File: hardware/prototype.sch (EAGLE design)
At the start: 33 parts, among them IC1 PCA82C251, IC2 ATMEGA328P-PU, Q3 BS170

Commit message: Smaller PCB, also the placement of the RASPI port has been corrected and the Serial port error
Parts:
- removed SW1: (no value), special:SW_DIP-4
- ATMEGA168-20PU: value ATMEGA328P-PU -> ATMEGA168V-10P
- MCP2551: value PCA82C251 -> PCA82C250
- OSC1: value (none) -> 16MHz
- renumbered IC1 to MCP2551, IC2 to ATMEGA168-20PU, ISP1 to ICSP, LED3 to RXBUF1, LED4 to RXBUF2, Q1 to 16MHZ, Q2 to OSC1, S1 to RESET, SV1 to RASPI, U$1 to MCP2515-I/P, X1 to CANPORT
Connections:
- removed net N$12: ATMEGA168-20PU.(PCI4/MISO)PB4, ICSP.MISO, SW1.3
- removed net N$13: ATMEGA168-20PU.(PCI3/MOSI/OC2A)PB3, ICSP.MOSI, SW1.2
- removed net N$14: ATMEGA168-20PU.(PCI5/SCK)PB5, ICSP.SCK, SW1.4
- removed net N$21: ATMEGA168-20PU.(PCI16/RXD)PD0, R4.1
- removed net N$28: ATMEGA168-20PU.(PCI2/SS/OC1B)PB2, SW1.1
- new net N$11: ATMEGA168-20PU.(PCI17/TXD)PD1, R4.1
- net N$10: now also ATMEGA168-20PU.(PCI2/SS/OC1B)PB2; no longer SW1.8
- net N$15: now also ATMEGA168-20PU.(PCI5/SCK)PB5, ICSP.SCK; no longer SW1.5
- net N$23: now also ATMEGA168-20PU.(PCI16/RXD)PD0; no longer ATMEGA168-20PU.(PCI17/TXD)PD1
- net N$26: now also ATMEGA168-20PU.(PCI4/MISO)PB4, ICSP.MISO; no longer SW1.6
- net N$27: now also ATMEGA168-20PU.(PCI3/MOSI/OC2A)PB3, ICSP.MOSI; no longer SW1.7

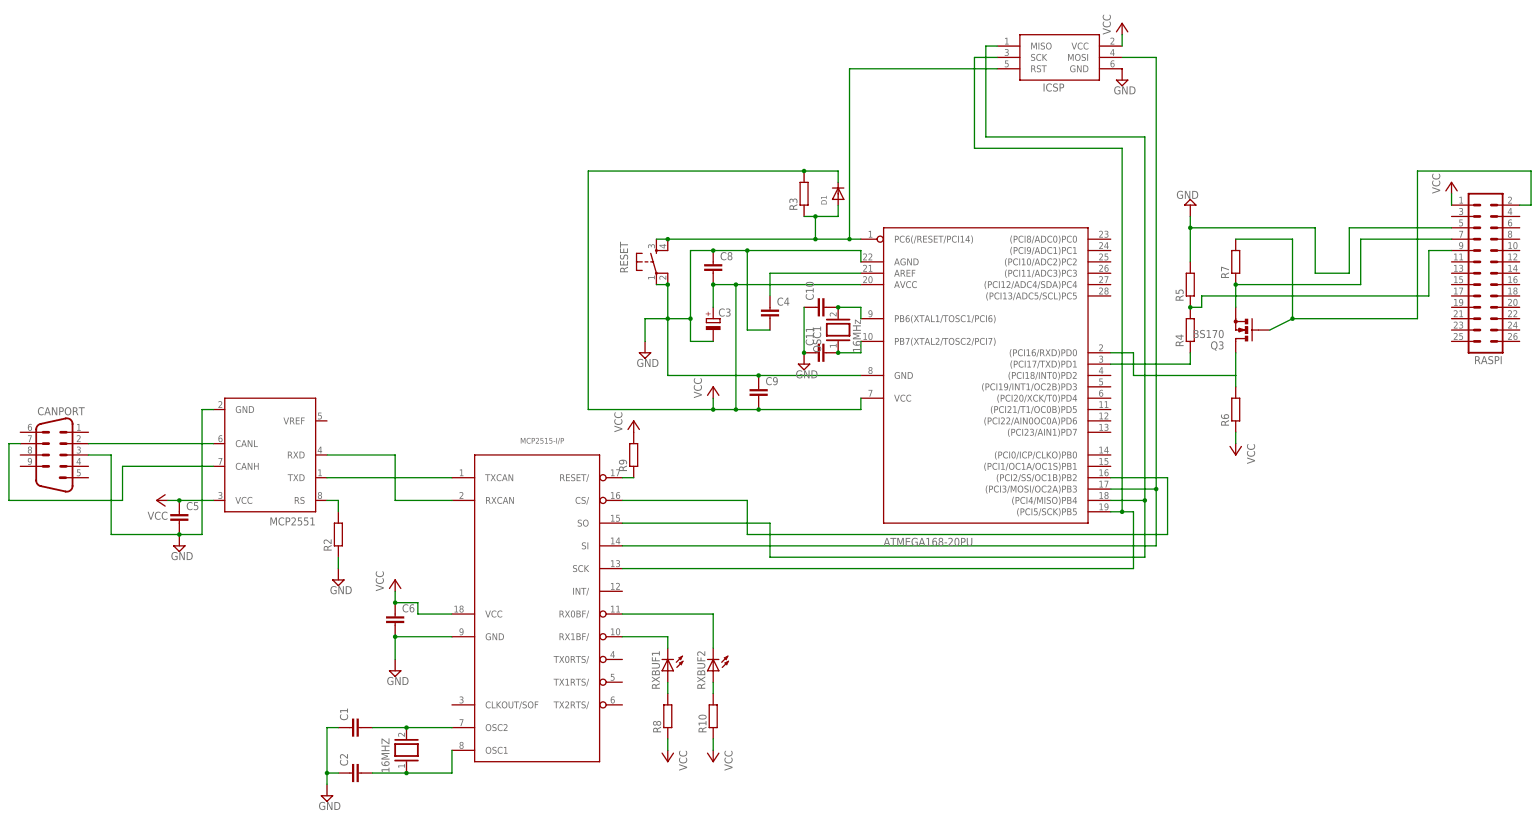
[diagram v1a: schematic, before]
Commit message: Added gerbers for DirtyPCBs and OSHpark.
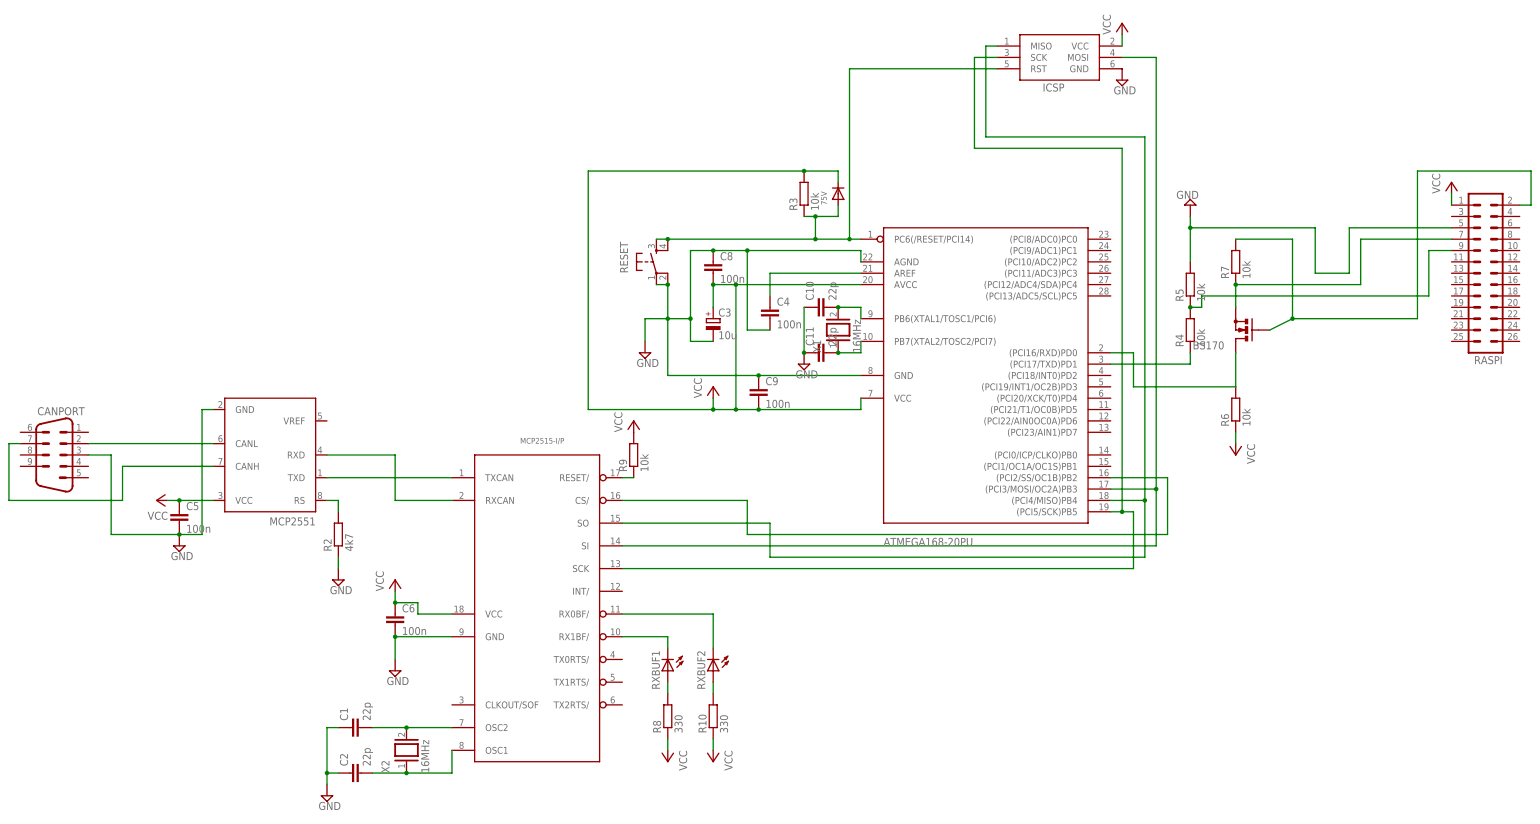
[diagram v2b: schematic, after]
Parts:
- C1, C10, C11, C2: value (none) -> 22p
- C3: value (none) -> 10u
- C4, C5, C6, C8, C9: value (none) -> 100n
- R10, R8: value (none) -> 330
- R2: value (none) -> 4k7
- R3, R4, R5, R6, R7, R9: value (none) -> 10k
- X2: value (none) -> 16MHz
- renumbered 16MHZ to X2, D1 to 75V, OSC1 to X1, Q3 to BS170
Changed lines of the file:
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@@
 <part name="P+7" library="supply1" deviceset="VCC" device=""/>
 <part name="SUPPLY5" library="supply2" deviceset="GND" device=""/>
-<part name="C5" library="rcl" deviceset="C-EU" device="050-025X075"/>
-<part name="C6" library="rcl" deviceset="C-EU" device="050-025X075"/>
-<part name="C1" library="rcl" deviceset="C-EU" device="050-025X075"/>
-<part name="C2" library="rcl" deviceset="C-EU" device="050-025X075"/>
-<part name="R2" library="rcl" deviceset="R-EU_" device="0204/7"/>
-<part name="R8" library="rcl" deviceset="R-EU_" device="0204/7"/>
-<part name="R9" library="rcl" deviceset="R-EU_" device="0204/7"/>
-<part name="R10" library="rcl" deviceset="R-EU_" device="0204/7"/>
-<part name="16MHZ" library="special" deviceset="XTAL/S" device=""/>
+<part name="C5" library="rcl" deviceset="C-EU" device="050-025X075" value="100n"/>
+<part name="C6" library="rcl" deviceset="C-EU" device="050-025X075" value="100n"/>
+<part name="C1" library="rcl" deviceset="C-EU" device="050-025X075" value="22p"/>
+<part name="C2" library="rcl" deviceset="C-EU" device="050-025X075" value="22p"/>
+<part name="R2" library="rcl" deviceset="R-EU_" device="0204/7" value="4k7"/>
+<part name="R8" library="rcl" deviceset="R-EU_" device="0204/7" value="330"/>
+<part name="R9" library="rcl" deviceset="R-EU_" device="0204/7" value="10k"/>
+<part name="R10" library="rcl" deviceset="R-EU_" device="0204/7" value="330"/>
+<part name="X2" library="special" deviceset="XTAL/S" device="" value="16MHz"/>
 <part name="ATMEGA168-20PU" library="adafruit" deviceset="ATMEGA168*P" device="" technology="V-10" value=""/>
-<part name="C4" library="rcl" deviceset="C-EU" device="050-025X075"/>
-<part name="C8" library="rcl" deviceset="C-EU" device="050-025X075"/>
-<part name="C9" library="rcl" deviceset="C-EU" device="050-025X075"/>
+<part name="C4" library="rcl" deviceset="C-EU" device="050-025X075" value="100n"/>
+<part name="C8" library="rcl" deviceset="C-EU" device="050-025X075" value="100n"/>
+<part name="C9" library="rcl" deviceset="C-EU" device="050-025X075" value="100n"/>
 <part name="RESET" library="switch-tact" deviceset="DTS-6" device="" value=""/>
 <part name="P+1" library="supply1" deviceset="VCC" device=""/>
 <part name="SUPPLY6" library="supply2" deviceset="GND" device=""/>
-<part name="C3" library="rcl" deviceset="CPOL-EU" device="E2-5"/>
-<part name="OSC1" library="special" deviceset="XTAL/S" device="" value="16MHz"/>
-<part name="C10" library="rcl" deviceset="C-EU" device="050-025X075"/>
-<part name="C11" library="rcl" deviceset="C-EU" device="050-025X075"/>
+<part name="C3" library="rcl" deviceset="CPOL-EU" device="E2-5" value="10u"/>
+<part name="X1" library="special" deviceset="XTAL/S" device="" value="16MHz"/>
+<part name="C10" library="rcl" deviceset="C-EU" device="050-025X075" value="22p"/>
+<part name="C11" library="rcl" deviceset="C-EU" device="050-025X075" value="22p"/>
 <part name="SUPPLY7" library="supply2" deviceset="GND" device=""/>
-<part name="R3" library="rcl" deviceset="R-EU_" device="0204/7"/>
-<part name="D1" library="adafruit" deviceset="DIODE" device="DO-1N4148"/>
-<part name="Q3" library="transistor-small-signal" deviceset="BS170" device=""/>
-<part name="R4" library="rcl" deviceset="R-EU_" device="0204/7"/>
-<part name="R5" library="rcl" deviceset="R-EU_" device="0204/7"/>
+<part name="R3" library="rcl" deviceset="R-EU_" device="0204/7" value="10k"/>
+<part name="75V" library="adafruit" deviceset="DIODE" device="DO-1N4148"/>
+<part name="BS170" library="transistor-small-signal" deviceset="BS170" device="" value=""/>
+<part name="R4" library="rcl" deviceset="R-EU_" device="0204/7" value="10k"/>
+<part name="R5" library="rcl" deviceset="R-EU_" device="0204/7" value="10k"/>
 <part name="SUPPLY8" library="supply2" deviceset="GND" device=""/>
-<part name="R6" library="rcl" deviceset="R-EU_" device="0204/7"/>
+<part name="R6" library="rcl" deviceset="R-EU_" device="0204/7" value="10k"/>
 <part name="P+2" library="supply1" deviceset="VCC" device=""/>
-<part name="R7" library="rcl" deviceset="R-EU_" device="0204/7"/>
+<part name="R7" library="rcl" deviceset="R-EU_" device="0204/7" value="10k"/>
 <part name="RASPI" library="con-lstb" deviceset="MA13-2" device=""/>
 <part name="ICSP" library="adafruit" deviceset="AVRISP" device="-6"/>
@@
 <instance part="R9" gate="G$1" x="142.24" y="63.5" rot="R90"/>
 <instance part="R10" gate="G$1" x="160.02" y="5.08" rot="R90"/>
-<instance part="16MHZ" gate="G$1" x="91.44" y="-2.54" rot="R90"/>
+<instance part="X2" gate="G$1" x="91.44" y="-2.54" rot="R90"/>
 <instance part="ATMEGA168-20PU" gate="G$1" x="215.9" y="83.82"/>
 <instance part="C4" gate="G$1" x="172.72" y="96.52"/>
@@
 <instance part="SUPPLY6" gate="GND" x="144.78" y="86.36"/>
 <instance part="C3" gate="G$1" x="160.02" y="93.98"/>
-<instance part="OSC1" gate="G$1" x="187.96" y="91.44" rot="R90"/>
+<instance part="X1" gate="G$1" x="187.96" y="91.44" rot="R90"/>
 <instance part="C10" gate="G$1" x="182.88" y="96.52" rot="R90"/>
 <instance part="C11" gate="G$1" x="182.88" y="86.36" rot="R90"/>
 <instance part="SUPPLY7" gate="GND" x="180.34" y="83.82"/>
 <instance part="R3" gate="G$1" x="180.34" y="121.92" rot="R90"/>
-<instance part="D1" gate="G$1" x="187.96" y="121.92" rot="R90"/>
-<instance part="Q3" gate="1" x="279.4" y="91.44" rot="R180"/>
+<instance part="75V" gate="G$1" x="187.96" y="121.92" rot="R90"/>
+<instance part="BS170" gate="1" x="279.4" y="91.44" rot="R180"/>
 <instance part="R4" gate="G$1" x="266.7" y="91.44" rot="R90"/>
 <instance part="R5" gate="G$1" x="266.7" y="101.6" rot="R90"/>
@@
 <wire x1="180.34" y1="127" x2="187.96" y2="127" width="0.1524" layer="91"/>
 <junction x="180.34" y="127"/>
-<pinref part="D1" gate="G$1" pin="C"/>
+<pinref part="75V" gate="G$1" pin="C"/>
 <wire x1="187.96" y1="127" x2="187.96" y2="124.46" width="0.1524" layer="91"/>
 </segment>
@@
 <wire x1="101.6" y1="2.54" x2="91.44" y2="2.54" width="0.1524" layer="91"/>
 <pinref part="C1" gate="G$1" pin="2"/>
-<pinref part="16MHZ" gate="G$1" pin="2"/>
+<pinref part="X2" gate="G$1" pin="2"/>
 <wire x1="91.44" y1="2.54" x2="83.82" y2="2.54" width="0.1524" layer="91"/>
 <junction x="91.44" y="2.54"/>
@@
 <pinref part="C2" gate="G$1" pin="2"/>
 <wire x1="101.6" y1="-7.62" x2="91.44" y2="-7.62" width="0.1524" layer="91"/>
-<pinref part="16MHZ" gate="G$1" pin="1"/>
+<pinref part="X2" gate="G$1" pin="1"/>
 <wire x1="91.44" y1="-7.62" x2="83.82" y2="-7.62" width="0.1524" layer="91"/>
 <junction x="91.44" y="-7.62"/>
@@
 <pinref part="ATMEGA168-20PU" gate="G$1" pin="PB6(XTAL1/TOSC1/PCI6)"/>
 <wire x1="193.04" y1="93.98" x2="193.04" y2="96.52" width="0.1524" layer="91"/>
-<pinref part="OSC1" gate="G$1" pin="2"/>
+<pinref part="X1" gate="G$1" pin="2"/>
 <wire x1="193.04" y1="96.52" x2="187.96" y2="96.52" width="0.1524" layer="91"/>
 <pinref part="C10" gate="G$1" pin="2"/>
@@
 <pinref part="ATMEGA168-20PU" gate="G$1" pin="PB7(XTAL2/TOSC2/PCI7)"/>
 <wire x1="193.04" y1="88.9" x2="193.04" y2="86.36" width="0.1524" layer="91"/>
-<pinref part="OSC1" gate="G$1" pin="1"/>
+<pinref part="X1" gate="G$1" pin="1"/>
 <wire x1="193.04" y1="86.36" x2="187.96" y2="86.36" width="0.1524" layer="91"/>
 <pinref part="C11" gate="G$1" pin="2"/>
@@
 <net name="N$23" class="0">
 <segment>
+<pinref part="ATMEGA168-20PU" gate="G$1" pin="(PCI16/RXD)PD0"/>
+<wire x1="248.92" y1="86.36" x2="254" y2="86.36" width="0.1524" layer="91"/>
+<wire x1="254" y1="86.36" x2="254" y2="78.74" width="0.1524" layer="91"/>
+<pinref part="BS170" gate="1" pin="D"/>
 <pinref part="R6" gate="G$1" pin="2"/>
-<pinref part="Q3" gate="1" pin="D"/>
-<wire x1="276.86" y1="86.36" x2="276.86" y2="81.28" width="0.1524" layer="91"/>
-<pinref part="ATMEGA168-20PU" gate="G$1" pin="(PCI16/RXD)PD0"/>
-<wire x1="276.86" y1="81.28" x2="276.86" y2="78.74" width="0.1524" layer="91"/>
-<wire x1="248.92" y1="86.36" x2="254" y2="86.36" width="0.1524" layer="91"/>
-<wire x1="254" y1="86.36" x2="254" y2="81.28" width="0.1524" layer="91"/>
-<wire x1="254" y1="81.28" x2="276.86" y2="81.28" width="0.1524" layer="91"/>
+<wire x1="276.86" y1="86.36" x2="276.86" y2="78.74" width="0.1524" layer="91"/>
+<wire x1="276.86" y1="78.74" x2="254" y2="78.74" width="0.1524" layer="91"/>
 </segment>
 </net>
@@
 <wire x1="276.86" y1="111.76" x2="289.56" y2="111.76" width="0.1524" layer="91"/>
 <wire x1="289.56" y1="111.76" x2="289.56" y2="93.98" width="0.1524" layer="91"/>
-<pinref part="Q3" gate="1" pin="G"/>
+<pinref part="BS170" gate="1" pin="G"/>
 <wire x1="284.48" y1="91.44" x2="289.56" y2="93.98" width="0.1524" layer="91"/>
 <wire x1="289.56" y1="93.98" x2="317.5" y2="93.98" width="0.1524" layer="91"/>
@@
 <net name="N$32" class="0">
 <segment>
-<pinref part="Q3" gate="1" pin="S"/>
+<pinref part="BS170" gate="1" pin="S"/>
 <pinref part="RASPI" gate="G$1" pin="7"/>
 <wire x1="325.12" y1="111.76" x2="304.8" y2="111.76" width="0.1524" layer="91"/>
@@
 <pinref part="R3" gate="G$1" pin="1"/>
 <wire x1="180.34" y1="116.84" x2="182.88" y2="116.84" width="0.1524" layer="91"/>
-<pinref part="D1" gate="G$1" pin="A"/>
+<pinref part="75V" gate="G$1" pin="A"/>
 <wire x1="182.88" y1="116.84" x2="187.96" y2="116.84" width="0.1524" layer="91"/>
 <wire x1="187.96" y1="116.84" x2="187.96" y2="119.38" width="0.1524" layer="91"/>
@@
 </sheet>
 </sheets>
+<errors>
+</errors>
 </schematic>
 </drawing>
